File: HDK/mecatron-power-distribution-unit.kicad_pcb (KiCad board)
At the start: 2 copper layers, 32 parts, among them J101 PwrIn_{1}, J102 PwrIn_{2}, J103 E-Stop, J104 PwrSw, J201 P1-Out, J202 P1-Out, J203 P1-Out, J204 P1-Out, J205 P1-Out, J206 P1-Out

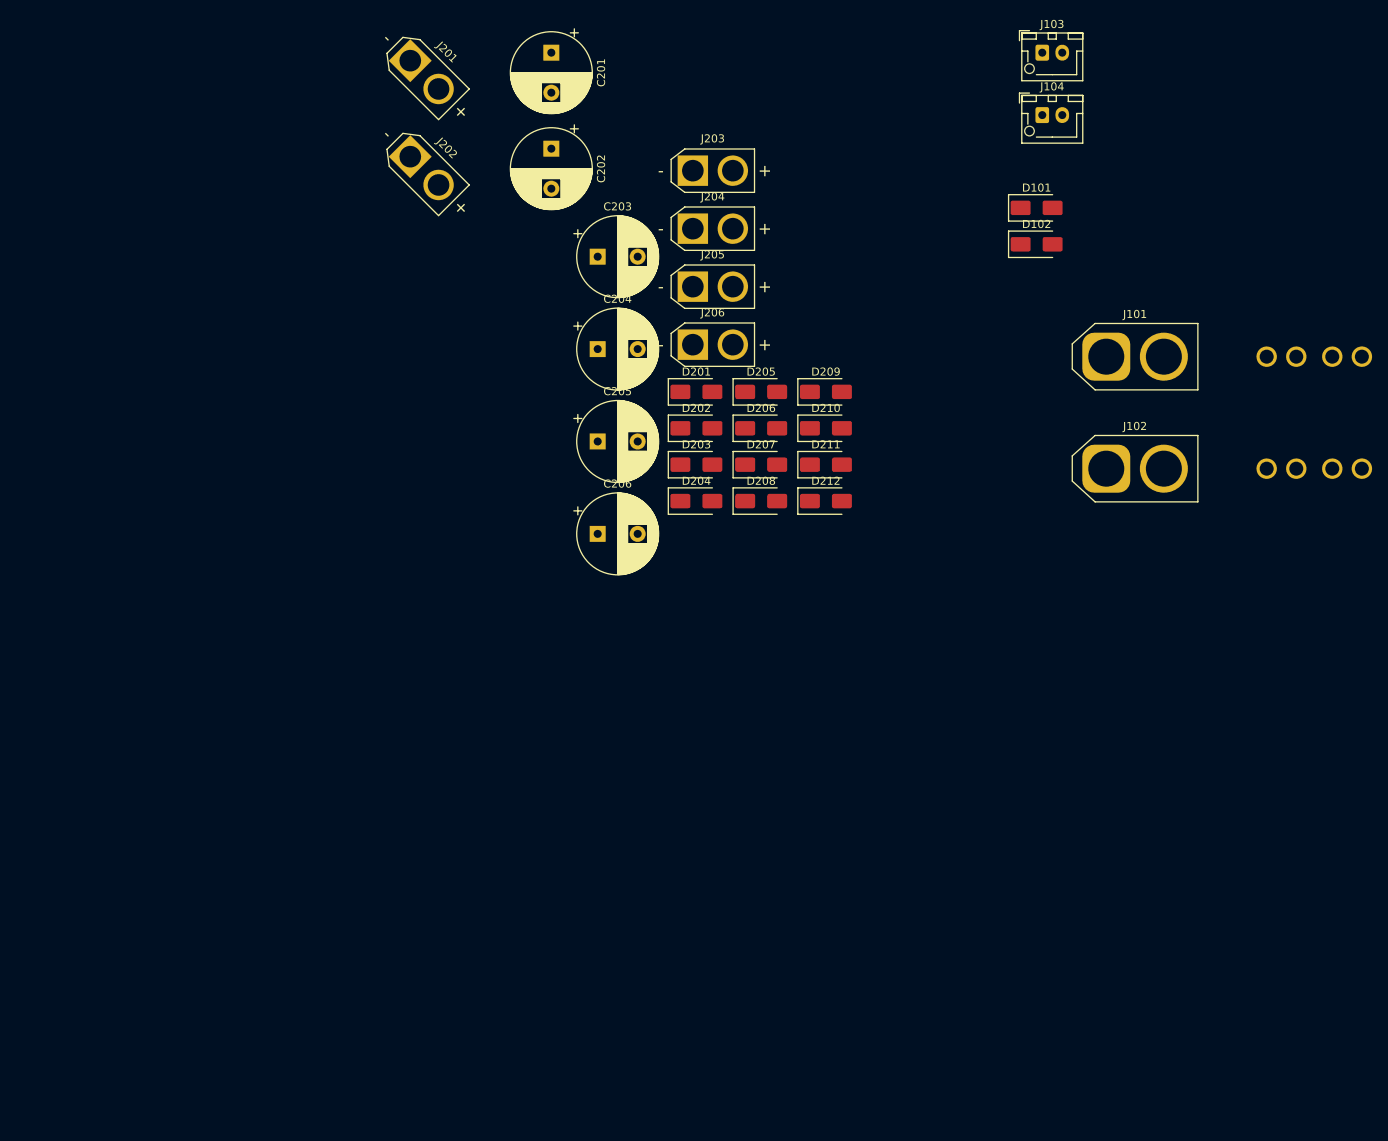
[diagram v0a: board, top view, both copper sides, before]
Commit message: added connectors
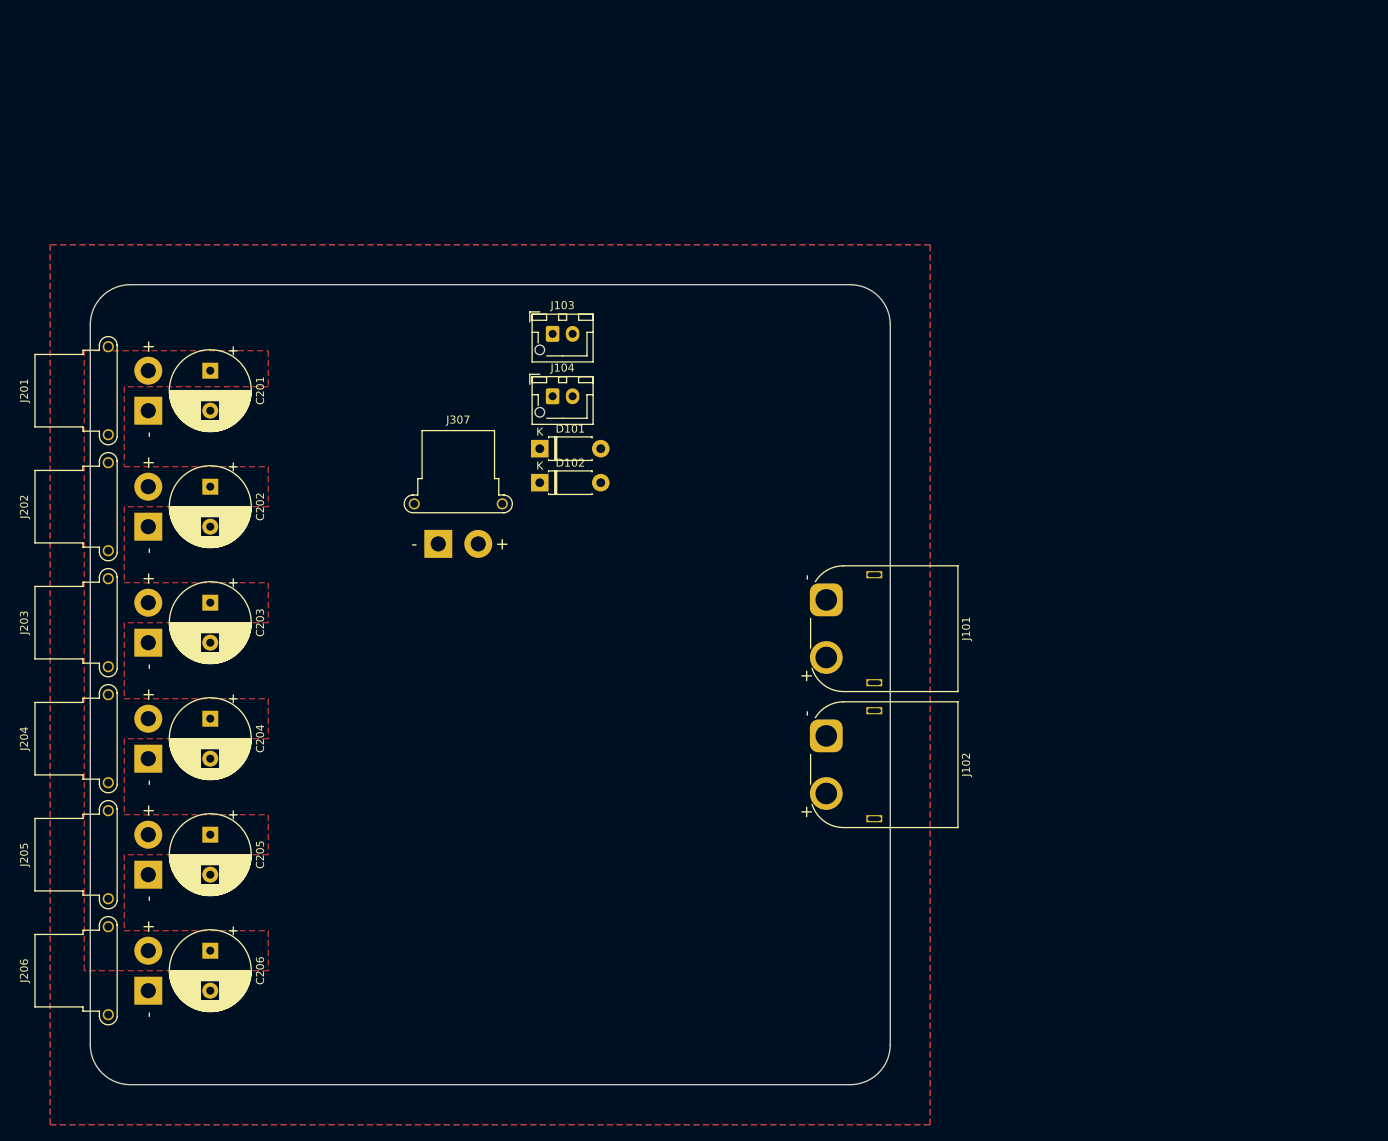
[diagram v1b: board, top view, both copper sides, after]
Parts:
- removed D201, D202, D203, D204, D205, D206, D207, D208, D209, D210, D211, D212: D_TVS, Diode_SMD:D_SMA
- removed F101, F102: 15A, NVF-Kicad:FUSE-MCCQ-122
- added J307: PwrOut_{2}, mecatron-kicad-footprints:AMASS_XT30PW-F_1x02_P2.50mm_Horizontal, F.Cu at (93.5, 82.4)
- C201, C202, C203, C204, C205, C206: value 470u -> 560u
- D101, D102: value D -> 1N4004; footprint Diode_SMD:D_SMA -> Diode_THT:D_DO-41_SOD81_P7.62mm_Horizontal
- J101, J102: footprint Connector_AMASS:AMASS_XT60-F_1x02_P7.20mm_Vertical -> mecatron-kicad-footprints:AMASS_XT60PW-M_1x02_P7.20mm_Horizontal
- J201, J202, J203, J204, J205, J206: footprint Connector_AMASS:AMASS_XT30U-M_1x02_P5.0mm_Vertical -> mecatron-kicad-footprints:AMASS_XT30PW-F_1x02_P2.50mm_Horizontal
- moved J206 105.6 mm to (57.2, 138.2), turned to 90 degrees
- moved J205 100.2 mm to (57.2, 123.8), turned to 90 degrees
- moved J204 95.0 mm to (57.2, 109.2), turned to 90 degrees
- moved J203 90.1 mm to (57.2, 94.8), turned to 90 degrees
- moved C206 71.1 mm to (65.0, 133.2), turned to -90 degrees
- moved J103 70.6 mm to (107.8, 56.1)
- moved J104 70.6 mm to (107.8, 64.0)
- moved D101 69.0 mm to (106.2, 70.5)
- moved C205 69.0 mm to (65.0, 118.8), turned to -90 degrees
- moved D102 68.9 mm to (106.2, 74.8)
- moved C204 66.9 mm to (65.0, 104.2), turned to -90 degrees
- moved C203 64.9 mm to (65.0, 89.8), turned to -90 degrees
- moved C202 60.0 mm to (65.0, 75.2)
- moved C201 58.3 mm to (65.0, 60.8)
- moved J202 56.7 mm to (57.2, 80.2), turned to 90 degrees
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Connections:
- J201 pad 1: VCCF_{Sec} -> GND
- J201 pad 2: GND -> VCCF_{Sec}
- J202 pad 1: VCCF_{Sec} -> GND
- J202 pad 2: GND -> VCCF_{Sec}
- J203 pad 1: VCCF_{Sec} -> GND
- J203 pad 2: GND -> VCCF_{Sec}
- J204 pad 1: VCCF_{Sec} -> GND
- J204 pad 2: GND -> VCCF_{Sec}
- J205 pad 1: VCCF_{Sec} -> GND
- J205 pad 2: GND -> VCCF_{Sec}
- J206 pad 1: VCCF_{Sec} -> GND
- J206 pad 2: GND -> VCCF_{Sec}
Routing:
- added copper zone on B.Cu, net GND
- added copper zone on F.Cu, net GND
- added copper zone on F.Cu, net VCCF_{Sec}
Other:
- board outline added: 100 x 100 mm
